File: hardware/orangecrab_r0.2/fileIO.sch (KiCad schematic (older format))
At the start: 33 parts, among them J1 Conn_01x12_Male, J2 Conn_01x16_Male, J3 USB_B_Micro, J7 Conn_02x15_Odd_Even, SW1 SW_Push, U9 ATSAMD11D14A

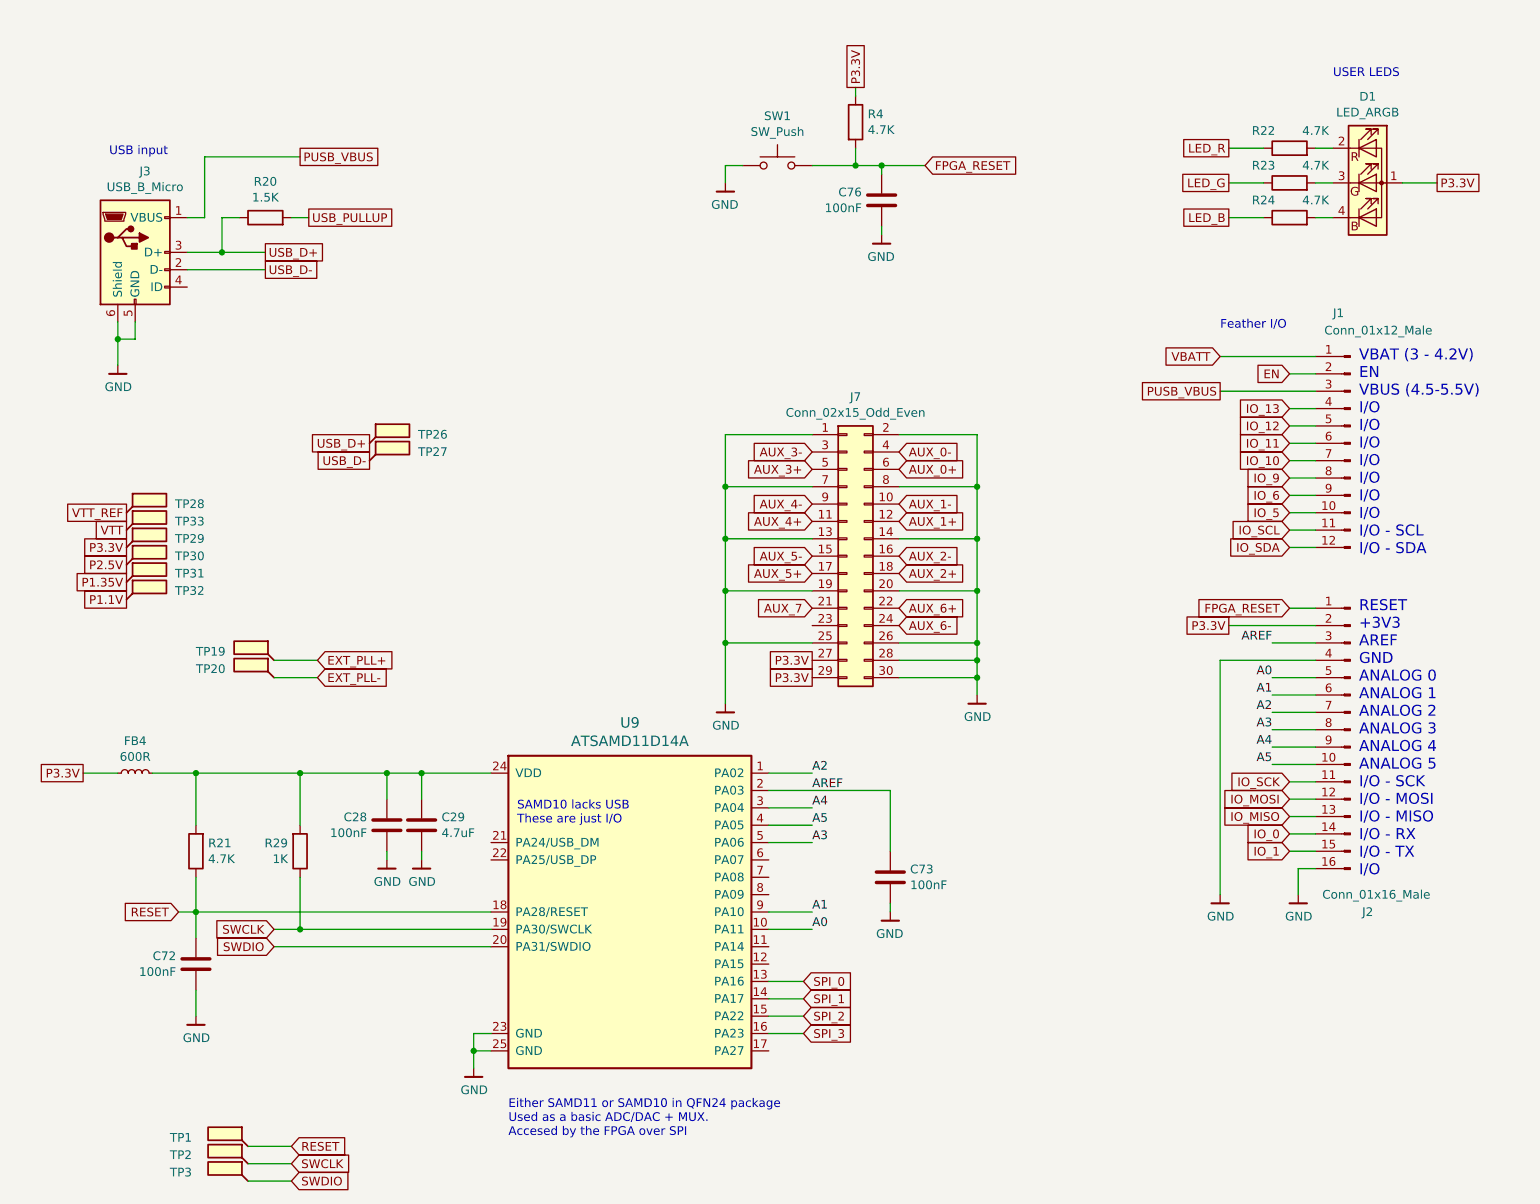
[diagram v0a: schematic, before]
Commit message: hw: Update I/O block routing new DDR3 signals.
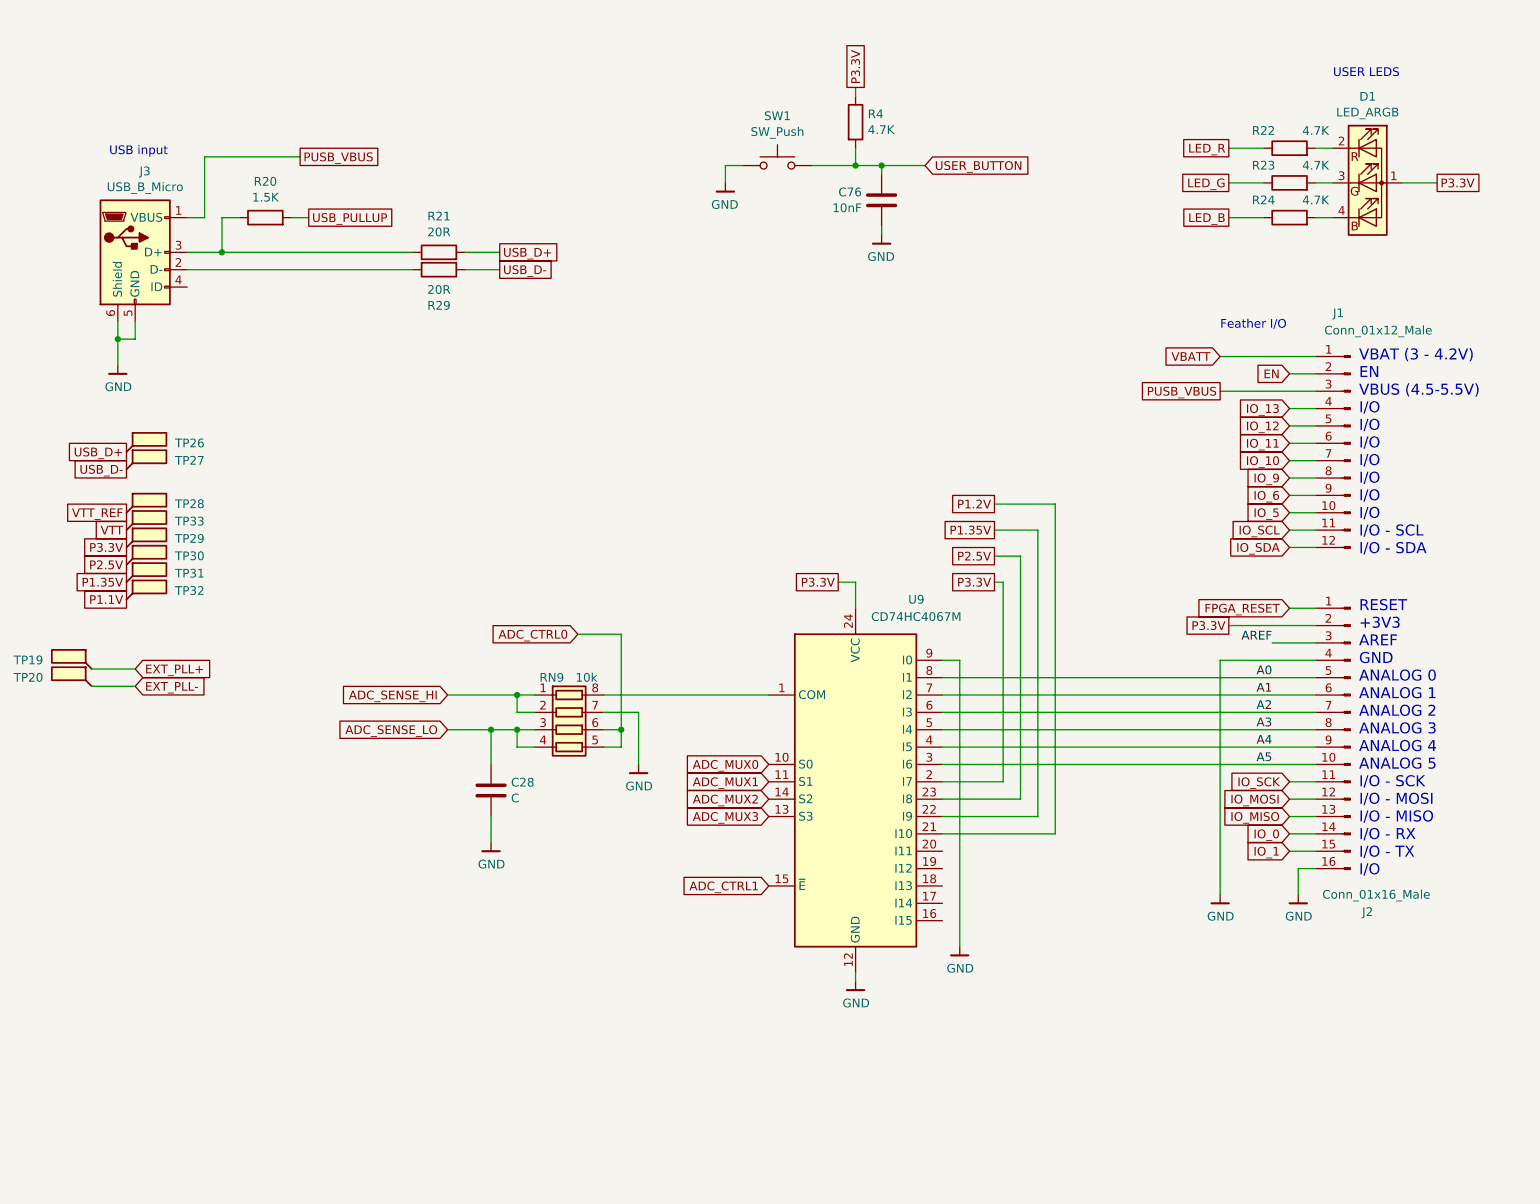
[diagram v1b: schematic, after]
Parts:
- removed C29: 4.7uF, Capacitor_SMD:C_0402_1005Metric, symbol Device:C
- removed C72, C73: 100nF, Capacitor_SMD:C_0201_0603Metric, symbol Device:C
- removed FB4: 600R, Inductor_SMD:L_0402_1005Metric, symbol Device:L_Small
- removed J7: Conn_02x15_Odd_Even, gkl_conn:DF12(3.0)-30DP-0.5V(86), symbol Connector_Generic:Conn_02x15_Odd_Even
- removed TP1, TP2, TP3: SMD_TP, gkl_misc:TestPoint_Pad_D0.5mm, symbol Connector:TestPoint_Flag
- removed U9: ATSAMD11D14A, Package_DFN_QFN:QFN-24-1EP_4x4mm_P0.5mm_EP2.6x2.6mm, symbol gkl_microchip:ATSAMD11D14A
- added RN9: 10k, Resistor_SMD:R_Array_Convex_4x0402, symbol Device:R_Pack04
- added U9: CD74HC4067M, Package_DFN_QFN:Texas_RGY_R-PVQFN-N24_EP2.05x3.1mm, symbol 74xx:CD74HC4067M
- C28: value 100nF -> C; footprint Capacitor_SMD:C_0201_0603Metric -> (none); Mfg Samsung Electro-Mechanics -> (none); PN CL03A104KQ3NNNC -> (none)
- C76: value 100nF -> 10nF; PN CL03A104KQ3NNNC -> CL03A103KQ3NNNC
- R21: value 4.7K -> 20R; PN RC0201FR-074K7L -> RC0201FR-071K5L
- R29: value 1K -> 20R; PN RC0201FR-071KL -> RC0201FR-071K5L
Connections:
- net SWCLK is gone; now on net USB_D-: R29.1
- net A0: now also U9.8 (I1)
- net A1: now also U9.7 (I2)
- net A2: now also U9.6 (I3)
- net A3: now also U9.5 (I4)
- net A4: now also U9.4 (I5)
- net A5: now also U9.3 (I6)
- net FPGA_RESET: no longer C76.1, R4.2, SW1.2
- net GND: now also RN9.7 (R2.2), U9.12 (GND), U9.9 (I0)
- net P1.35V: now also U9.22 (I9)
- net P2.5V: now also U9.23 (I8)
- net P3.3V: now also U9.2 (I7), U9.24 (VCC)
- net USB_D+: now also R21.2; no longer J3.3 (D+), R20.1
- net USB_D-: no longer J3.2 (D-)
- net RESET: no longer names the net of R21.1
- net RESET: now also J3.3 (D+), R20.1
- new net: J3.2 (D-), R29.2
- new net: RN9.8 (R1.2), U9.1 (COM)
- new net ADC_CTRL0: RN9.5 (R4.2), RN9.6 (R3.2)
- new net ADC_CTRL1: U9.15 (~E)
- new net ADC_MUX0: U9.10 (S0)
- new net ADC_MUX1: U9.11 (S1)
- new net ADC_MUX2: U9.14 (S2)
- new net ADC_MUX3: U9.13 (S3)
- new net ADC_SENSE_HI: RN9.1 (R1.1), RN9.2 (R2.1)
- new net ADC_SENSE_LO: C28.1, RN9.3 (R3.1), RN9.4 (R4.1)
- new net P1.2V: U9.21 (I10)
- new net USER_BUTTON: C76.1, R4.2, SW1.2
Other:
- note removed: "Either SAMD11 or SAMD10 in QFN24 package\nUsed as a basic ADC/DAC + MUX.\nAccesed by the FPGA over SPI"
- note removed: "SAMD10 lacks USB\nThese are just I/O\n"
- moved on the sheet: TP19, TP20, TP26, TP27

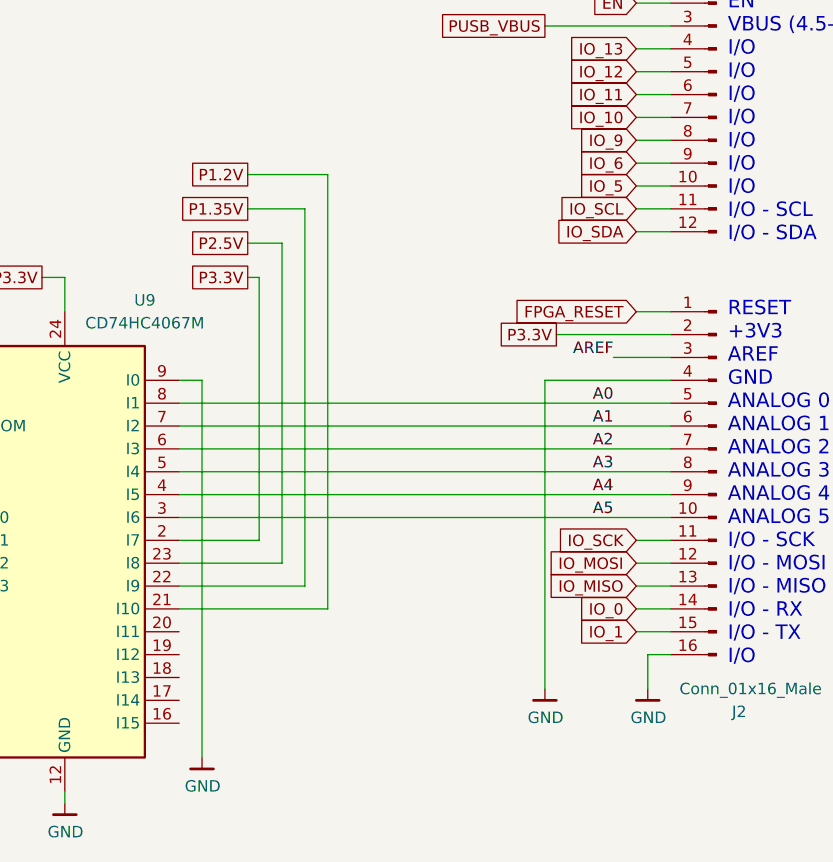
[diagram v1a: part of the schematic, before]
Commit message: hw: Routed analog section General cleanup
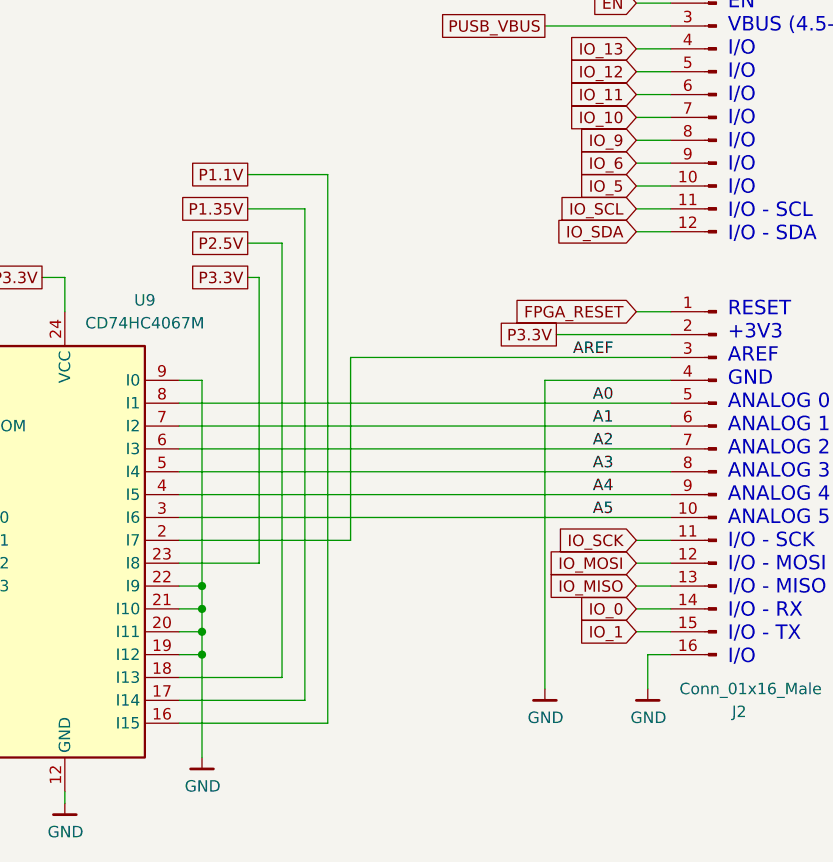
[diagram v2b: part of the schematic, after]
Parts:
- C28: footprint (none) -> Capacitor_SMD:C_0201_0603Metric
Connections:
- net P1.2V is gone; now on net GND: U9.21 (I10)
- net AREF: now also U9.2 (I7)
- net GND: now also U9.19 (I12), U9.20 (I11), U9.22 (I9)
- net P1.1V: now also U9.16 (I15)
- net P1.35V: now also U9.17 (I14); no longer U9.22 (I9)
- net P2.5V: now also U9.18 (I13); no longer U9.23 (I8)
- net P3.3V: now also U9.23 (I8); no longer U9.2 (I7)
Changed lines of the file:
@@
 Text Label 8350 4200 2    50   ~ 0
 A0
-Wire Wire Line
-	8600 4000 8350 4000
 Text Label 8350 4000 2    50   ~ 0
 AREF
@@
 $EndComp
 Wire Wire Line
-	6550 5750 6550 4100
+	6550 5750 6550 5300
 Wire Wire Line
 	6550 4100 6450 4100
@@
 	5950 3650 5950 3800
 Wire Wire Line
-	6450 4800 6800 4800
-Wire Wire Line
-	6450 4900 6900 4900
-Wire Wire Line
-	6450 5000 7000 5000
+	6450 5400 6900 5400
+Wire Wire Line
+	6450 5500 7000 5500
 Text GLabel 6750 3650 0    50   UnSpc ~ 0
 P3.3V
@@
 	6800 3650 6750 3650
 Wire Wire Line
-	6800 3650 6800 4800
+	6800 3650 6800 4900
 Text GLabel 6750 3500 0    50   UnSpc ~ 0
 P2.5V
@@
 	6750 3500 6900 3500
 Wire Wire Line
-	6900 3500 6900 4900
+	6900 3500 6900 5400
 Wire Wire Line
 	7000 3350 6750 3350
 Wire Wire Line
-	7000 3350 7000 5000
+	7000 3350 7000 5500
 Text GLabel 6750 3350 0    50   UnSpc ~ 0
 P1.35V
@@
 	7100 3200 6750 3200
 Text GLabel 6750 3200 0    50   UnSpc ~ 0
-P1.2V
-Wire Wire Line
-	7100 5100 6450 5100
-Wire Wire Line
-	7100 3200 7100 5100
+P1.1V
+Wire Wire Line
+	7100 5600 6450 5600
+Wire Wire Line
+	7100 3200 7100 5600
 Text GLabel 5450 4700 0    50   Input ~ 0
 ADC_MUX0
@@
 F 0 "C28" H 3965 4896 50  0000 L CNN
 F 1 "C" H 3965 4805 50  0000 L CNN
-F 2 "" H 3888 4700 50  0001 C CNN
+F 2 "Capacitor_SMD:C_0201_0603Metric" H 3888 4700 50  0001 C CNN
 F 3 "~" H 3850 4850 50  0001 C CNN
 	1    3850 4850
@@
 Wire Wire Line
 	3600 4300 4000 4300
+Wire Wire Line
+	6450 5000 6550 5000
+Connection ~ 6550 5000
+Wire Wire Line
+	6450 5100 6550 5100
+Connection ~ 6550 5100
+Wire Wire Line
+	6550 5100 6550 5000
+Wire Wire Line
+	6550 5200 6450 5200
+Connection ~ 6550 5200
+Wire Wire Line
+	6550 5200 6550 5100
+Wire Wire Line
+	6450 4800 7200 4800
+Wire Wire Line
+	7200 4800 7200 4000
+Wire Wire Line
+	7200 4000 8600 4000
+Wire Wire Line
+	6550 4100 6550 5000
+Wire Wire Line
+	6800 4900 6450 4900
+Wire Wire Line
+	6450 5300 6550 5300
+Connection ~ 6550 5300
+Wire Wire Line
+	6550 5300 6550 5200
 $EndSCHEMATC
